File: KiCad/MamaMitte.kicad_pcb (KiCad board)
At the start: 2 copper layers, 62 x 37.3 mm, 0 parts

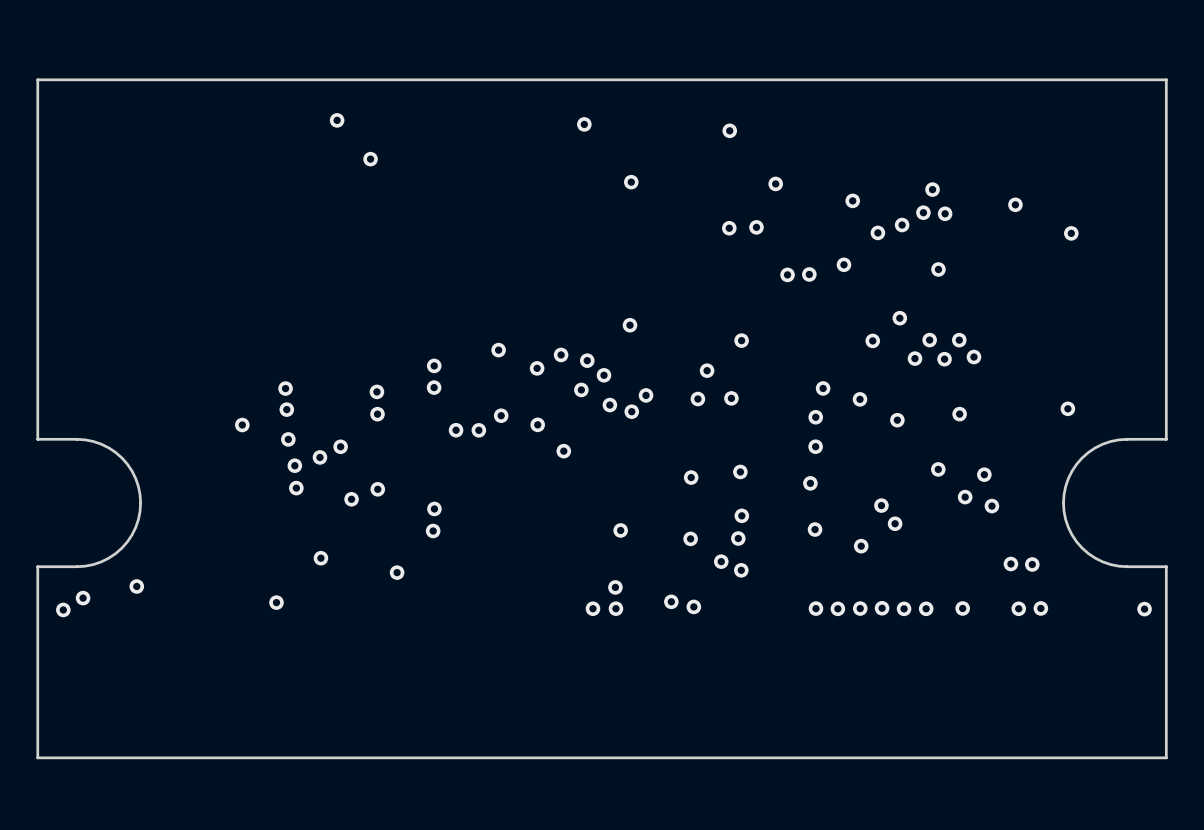
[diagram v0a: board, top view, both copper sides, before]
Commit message: Add footprints and assign nets
Assigned and placed footprints, and assigned nets to vias.
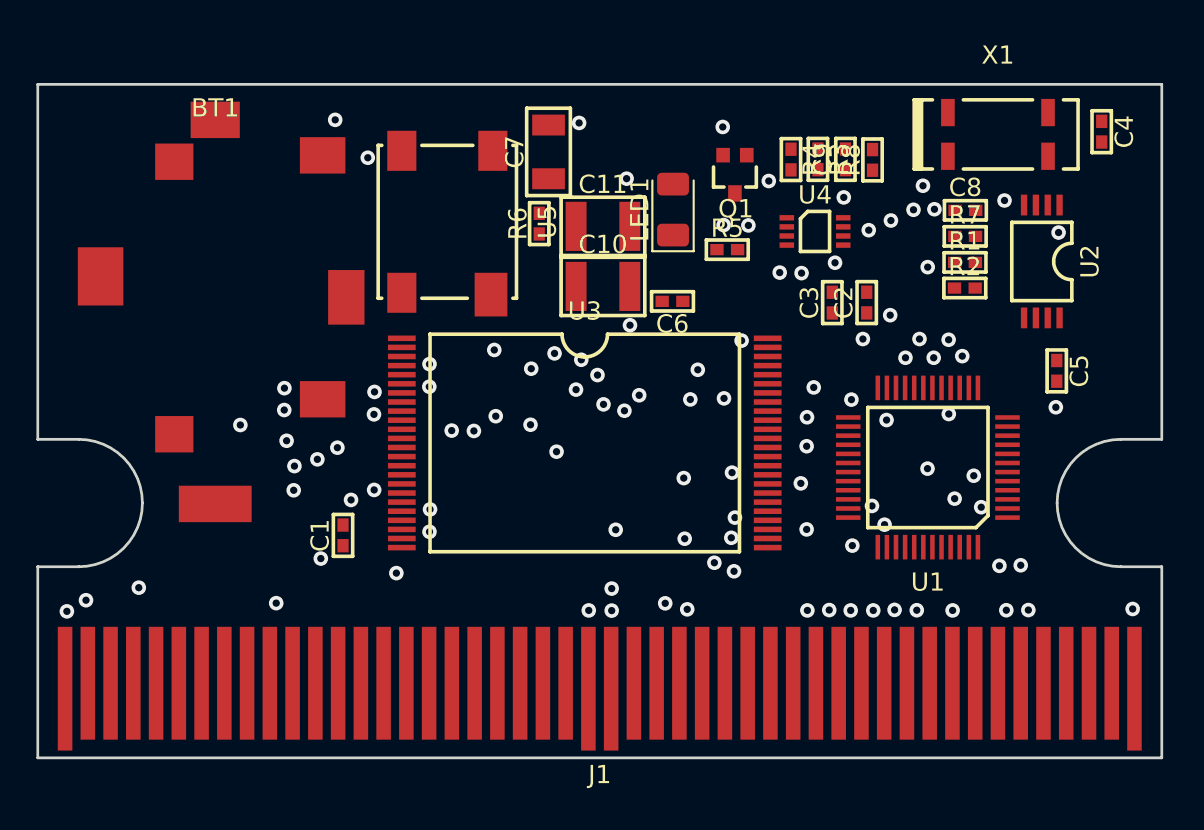
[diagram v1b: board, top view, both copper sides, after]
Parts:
- added BT1: CR1616, MamaMitte:BatteryHolder_3N1_CR1616, F.Cu at (109.8, 75.5)
- added C1: C105, MamaMitte:C_0402_1005Metric, F.Cu at (116.8, 87.8)
- added C10: C106, MamaMitte:C_1210_3225Metric, F.Cu at (131.1, 74.1)
- added C11: C106, MamaMitte:C_1210_3225Metric, F.Cu at (131.1, 70.8)
- added C2: C105, MamaMitte:C_0402_1005Metric, F.Cu at (145.5, 75.0)
- added C3: C103, MamaMitte:C_0402_1005Metric, F.Cu at (143.7, 75.0)
- added C4: C609, MamaMitte:C_0402_1005Metric, F.Cu at (158.4, 65.6)
- added C5: C103, MamaMitte:C_0402_1005Metric, F.Cu at (156.0, 78.7)
- added C6: C104, MamaMitte:C_0402_1005Metric, F.Cu at (134.9, 74.9)
- added C7: C, MamaMitte:C_1206_3216Metric, F.Cu at (128.1, 66.7)
- added C8: C105, MamaMitte:C_0402_1005Metric, F.Cu at (151.0, 69.9)
- added C9: C103, MamaMitte:C_0402_1005Metric, F.Cu at (144.4, 67.1)
- added J1: WSCART, MamaMitte:WSCE-48_P1.25mm, F.Cu at (130.9, 96.2)
- added LED1: D, LED_SMD:LED_1206_3216Metric, F.Cu at (134.9, 69.9)
- added Q1: 2SC4097, MamaMitte:SOT-323_SC-70, F.Cu at (138.3, 67.9)
- added R1: R103, MamaMitte:R_0402_1005Metric, F.Cu at (150.9, 72.8)
- added R2: R103, MamaMitte:R_0402_1005Metric, F.Cu at (150.9, 74.2)
- added R3: R, MamaMitte:R_0402_1005Metric, F.Cu at (142.9, 67.1)
- added R4: R, MamaMitte:R_0402_1005Metric, F.Cu at (141.4, 67.1)
- added R5: R, MamaMitte:R_0402_1005Metric, F.Cu at (137.9, 72.1)
- added R6: R, MamaMitte:R_0402_1005Metric, F.Cu at (127.5, 70.7)
- added R7: R, MamaMitte:R_0402_1005Metric, F.Cu at (150.9, 71.3)
- added R8: R, MamaMitte:R_0402_1005Metric, F.Cu at (145.9, 67.2)
- added U1: BANDAI2003, MamaMitte:LQFP-48_7x7mm_P0.5mm, F.Cu at (148.9, 84.0)
- added U2: S3511A, MamaMitte:SSOP-8_4.4x3mm_P0.65mm, F.Cu at (155.2, 72.7)
- added U3: MBM29LV800TA, MamaMitte:TSOP-I-48_18.4x12mm_P0.5mm, F.Cu at (130.1, 82.7)
- added U4: TC7W04FK, MamaMitte:SSOP-8_2.3x2mm_P0.5mm, F.Cu at (142.7, 71.1)
- added U5: TFMM53xx, MamaMitte:Vishay_TFMM5xx0, F.Cu at (122.5, 70.5)
- added X1: SPT2AF-6PF20PPM, MamaMitte:Oscillator_SMD_SeikoEpson_SPT2AF-4Pin_8.7x3.7mm, F.Cu at (152.8, 65.8)
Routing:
- net WE: vias 0 -> 2
- net RST: vias 0 -> 2
- net Q9: vias 0 -> 2
- net Q8: vias 0 -> 2
- net Q13: vias 0 -> 2
- net Q12: vias 0 -> 2
- net Q11: vias 0 -> 2
- net Q10: vias 0 -> 2
- net OE: vias 0 -> 2
- net IO1: vias 0 -> 2
- net IO0: vias 0 -> 2
- net INT: vias 0 -> 2
- net GND: vias 0 -> 31
- net CE: vias 0 -> 2
- net A9: vias 0 -> 2
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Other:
- board size 62 x 37.3 mm -> 61.8 x 37 mm
- rule pad_to_mask_clearance: 0 -> 0.15

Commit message: Add bottom traces and ground plane
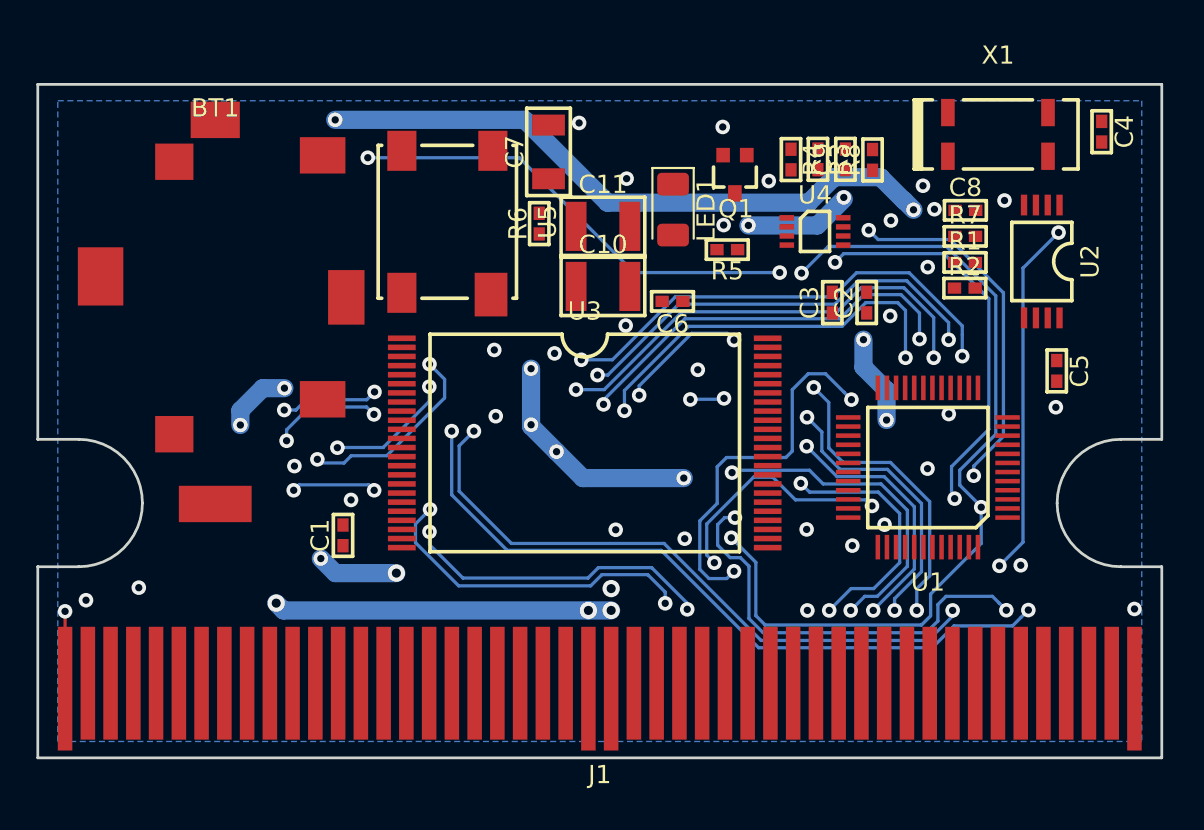
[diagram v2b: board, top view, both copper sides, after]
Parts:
- turned LED1 to 270 degrees
- turned R5 to 180 degrees
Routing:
- net GND: track 0.00 -> 51.3 mm, vias 31 -> 33
- net +3V3: track 0.00 -> 46.6 mm, vias 12 -> 13
- net WE: track 0.00 -> 39.5 mm
- net /Real-Time Clock/VBAT: track 0.00 -> 38.7 mm
- net RST: track 0.00 -> 35.0 mm
- net A15: track 0.00 -> 25.8 mm
- net /Infrared/RX: track 0.00 -> 25.2 mm
- net /Memory/A19: track 0.00 -> 24.9 mm
- net OE: track 0.00 -> 23.5 mm
- net /Memory/A20: track 0.00 -> 23.3 mm
- net A18: track 0.00 -> 21.8 mm
- net IO1: track 0.00 -> 21.6 mm
- net A17: track 0.00 -> 21.3 mm
- net CE: track 0.00 -> 20.4 mm
- net INT: track 0.00 -> 19.7 mm
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- added copper zone on B.Cu, net GND
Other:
- net class Default: trace_width 0.25 -> 0.18; via_dia 0.8 -> 0.95; via_drill 0.4 -> 0.5
- net class Power added: clearance 0.2, trace_width 1, via_dia 0.95, via_drill 0.5
- rule trace_min: 0.2 -> 0.1

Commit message: Resize vias
Use the via net class size.
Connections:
- J1 pad 0: (no net) -> GND
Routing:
- net GND: track 51.3 -> 58.9 mm, vias 33 -> 34
- net Q8: track 0.00 -> 4.45 mm
- net (no net): vias 3 -> 2
